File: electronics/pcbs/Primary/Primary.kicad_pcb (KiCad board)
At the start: 2 copper layers, 104.1 x 53.3 mm, 30 parts, among them J1 Line Sensor 1, J11 I2C Bus, J12 Battery, J13 Pololu_D24V50F5, J14 Magnet, J2 Line Sensor 2, J3 Line Sensor 3, J4 Line Sensor 4, J5 Line Sensor 5, J6 Line Sensor 6, J7 Servo, J8 Pololu_DRV8834, J9 Stepper Motor, P1 Digital, P10 CONN_01X01, P11 CONN_01X01, P12 CONN_01X01, P13 CONN_01X01, P2 Power, P3 Analog, P4 Analog, P5 PWM, P6 PWM, P7 Communication, P8 CONN_01X01, P9 CONN_01X01, Q1 Q_NPN_BCE

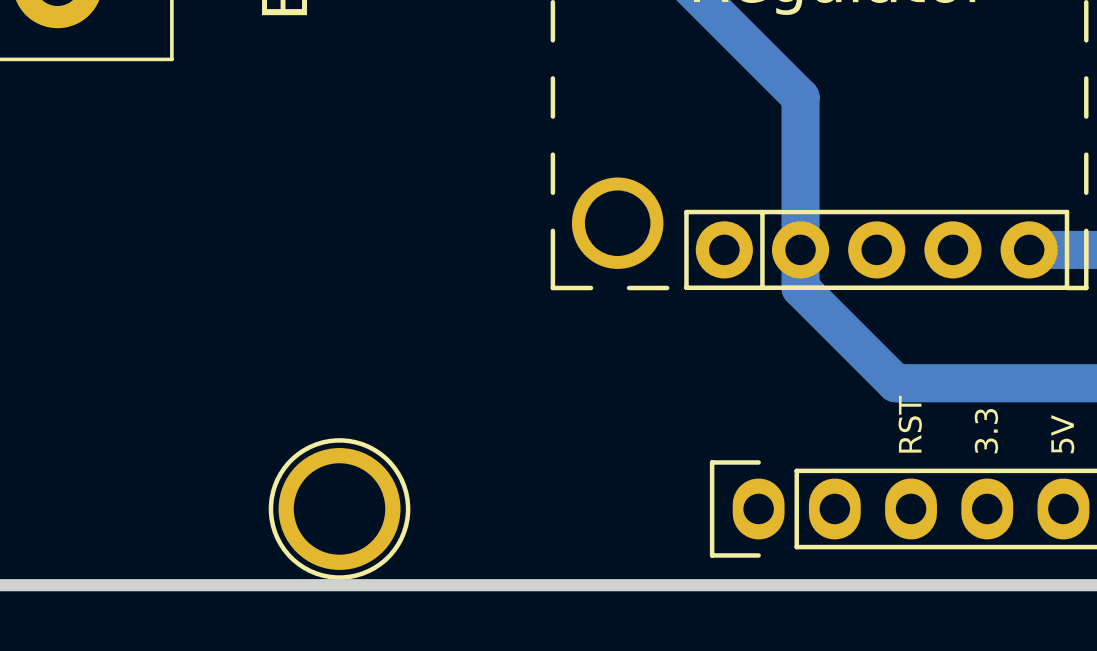
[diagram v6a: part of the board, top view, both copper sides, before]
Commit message: Primary PCB: Added Reset button.
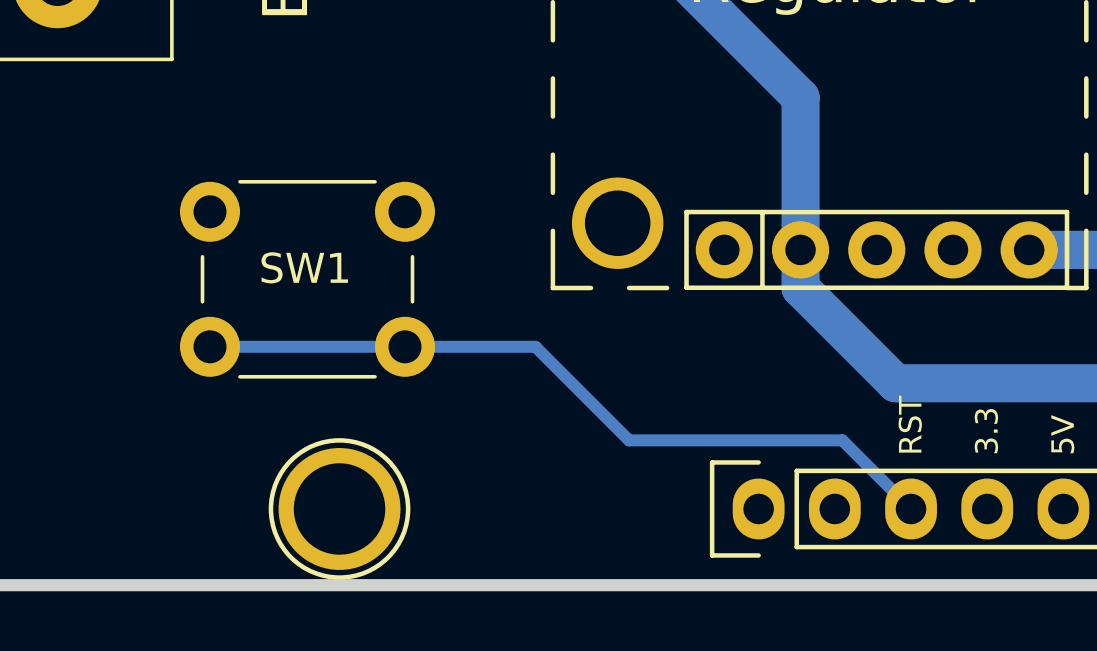
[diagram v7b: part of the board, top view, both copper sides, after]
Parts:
- added SW1: SW_Push, Buttons_Switches_THT:SW_PUSH_6mm_h4.3mm, F.Cu at (113.0, 109.2)
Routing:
- net /Reset: track 0.00 -> 25.6 mm
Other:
- board text added: "Reset"
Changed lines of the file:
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@@
 (kicad_pcb (version 4) (host pcbnew 4.0.7)
   (general
-    (links 60)
+    (links 64)
     (no_connects 1)
     (area 96.952999 66.743 207.721201 123.095)
     (thickness 1.6)
-    (drawings 178)
-    (tracks 74)
+    (drawings 179)
+    (tracks 79)
     (zones 0)
-    (modules 30)
+    (modules 31)
     (nets 94)
   )
@@
     (visible_elements 7FFEFF7F)
     (pcbplotparams
-      (layerselection 0x010f0_80000001)
-      (usegerberextensions true)
-      (excludeedgelayer true)
+      (layerselection 0x00200_00000000)
+      (usegerberextensions false)
+      (excludeedgelayer false)
       (linewidth 0.100000)
       (plotframeref false)
@@
       (padsonsilk false)
       (subtractmaskfromsilk false)
-      (outputformat 1)
+      (outputformat 5)
       (mirror false)
       (drillshape 0)
@@
     )
   )
+  (module Buttons_Switches_THT:SW_PUSH_6mm_h4.3mm (layer F.Cu)
+    (at 113.03 109.22)
+    (descr "tactile push button, 6x6mm e.g. PHAP33xx series, height=4.3mm")
+    (tags "tact sw push 6mm")
+    (fp_text reference SW1 (at 3.175 1.905) (layer F.SilkS)
+      (effects (font (size 1 1) (thickness 0.15)))
+    )
+    (fp_text value SW_Push (at 3.75 6.7) (layer F.Fab)
+      (effects (font (size 1 1) (thickness 0.15)))
+    )
+    (fp_text user %R (at 3.25 2.25) (layer F.Fab)
+      (effects (font (size 1 1) (thickness 0.15)))
+    )
+    (fp_line (start 3.25 -0.75) (end 6.25 -0.75) (layer F.Fab) (width 0.1))
+    (fp_line (start 6.25 -0.75) (end 6.25 5.25) (layer F.Fab) (width 0.1))
+    (fp_line (start 6.25 5.25) (end 0.25 5.25) (layer F.Fab) (width 0.1))
+    (fp_line (start 0.25 5.25) (end 0.25 -0.75) (layer F.Fab) (width 0.1))
+    (fp_line (start 0.25 -0.75) (end 3.25 -0.75) (layer F.Fab) (width 0.1))
+    (fp_line (start 7.75 6) (end 8 6) (layer F.CrtYd) (width 0.05))
+    (fp_line (start 8 6) (end 8 5.75) (layer F.CrtYd) (width 0.05))
+    (fp_line (start 7.75 -1.5) (end 8 -1.5) (layer F.CrtYd) (width 0.05))
+    (fp_line (start 8 -1.5) (end 8 -1.25) (layer F.CrtYd) (width 0.05))
+    (fp_line (start -1.5 -1.25) (end -1.5 -1.5) (layer F.CrtYd) (width 0.05))
+    (fp_line (start -1.5 -1.5) (end -1.25 -1.5) (layer F.CrtYd) (width 0.05))
+    (fp_line (start -1.5 5.75) (end -1.5 6) (layer F.CrtYd) (width 0.05))
+    (fp_line (start -1.5 6) (end -1.25 6) (layer F.CrtYd) (width 0.05))
+    (fp_line (start -1.25 -1.5) (end 7.75 -1.5) (layer F.CrtYd) (width 0.05))
+    (fp_line (start -1.5 5.75) (end -1.5 -1.25) (layer F.CrtYd) (width 0.05))
+    (fp_line (start 7.75 6) (end -1.25 6) (layer F.CrtYd) (width 0.05))
+    (fp_line (start 8 -1.25) (end 8 5.75) (layer F.CrtYd) (width 0.05))
+    (fp_line (start 1 5.5) (end 5.5 5.5) (layer F.SilkS) (width 0.12))
+    (fp_line (start -0.25 1.5) (end -0.25 3) (layer F.SilkS) (width 0.12))
+    (fp_line (start 5.5 -1) (end 1 -1) (layer F.SilkS) (width 0.12))
+    (fp_line (start 6.75 3) (end 6.75 1.5) (layer F.SilkS) (width 0.12))
+    (fp_circle (center 3.25 2.25) (end 1.25 2.5) (layer F.Fab) (width 0.1))
+    (pad 2 thru_hole circle (at 0 4.5 90) (size 2 2) (drill 1.1) (layers *.Cu *.Mask)
+      (net 36 /Reset))
+    (pad 1 thru_hole circle (at 0 0 90) (size 2 2) (drill 1.1) (layers *.Cu *.Mask)
+      (net 1 GND))
+    (pad 2 thru_hole circle (at 6.5 4.5 90) (size 2 2) (drill 1.1) (layers *.Cu *.Mask)
+      (net 36 /Reset))
+    (pad 1 thru_hole circle (at 6.5 0 90) (size 2 2) (drill 1.1) (layers *.Cu *.Mask)
+      (net 1 GND))
+    (model ${KISYS3DMOD}/Buttons_Switches_THT.3dshapes/SW_PUSH_6mm_h4.3mm.wrl
+      (at (xyz 0.005 0 0))
+      (scale (xyz 0.3937 0.3937 0.3937))
+      (rotate (xyz 0 0 0))
+    )
+  )
+  (gr_text Reset (at 116.205 106.045) (layer Cmts.User)
+    (effects (font (size 1.651 1.651) (thickness 0.4064)))
+  )
   (gr_circle (center 146.05 81.915) (end 146.05 83.185) (layer Cmts.User) (width 0.4064))
   (gr_text - (at 134.62 75.565) (layer Cmts.User)
@@
   (segment (start 184.785 108.585) (end 184.785 104.14) (width 1.27) (layer B.Cu) (net 34) (status 10))
   (segment (start 151.13 81.915) (end 151.13 78.74) (width 1.27) (layer B.Cu) (net 34))
+  (segment (start 136.398 119.126) (end 134.112 116.84) (width 0.4) (layer B.Cu) (net 36))
+  (segment (start 123.88 113.72) (end 119.53 113.72) (width 0.4) (layer B.Cu) (net 36))
+  (segment (start 127 116.84) (end 123.88 113.72) (width 0.4) (layer B.Cu) (net 36))
+  (segment (start 134.112 116.84) (end 127 116.84) (width 0.4) (layer B.Cu) (net 36))
+  (segment (start 113.03 113.72) (end 119.53 113.72) (width 0.4) (layer B.Cu) (net 36))
   (segment (start 132.08 78.74) (end 132.08 77.47) (width 0.4) (layer B.Cu) (net 57))
   (segment (start 134.874 74.676) (end 134.874 70.866) (width 0.4) (layer B.Cu) (net 57))
